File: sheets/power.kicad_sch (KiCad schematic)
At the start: 59 parts, among them J101 USB_C_Receptacle_USB2.0_16P, U102 TPS562201DDCT, U103 TPS562201DDCT, U104 TPS562201DDCT, U201 SAM9X60-V/DWB

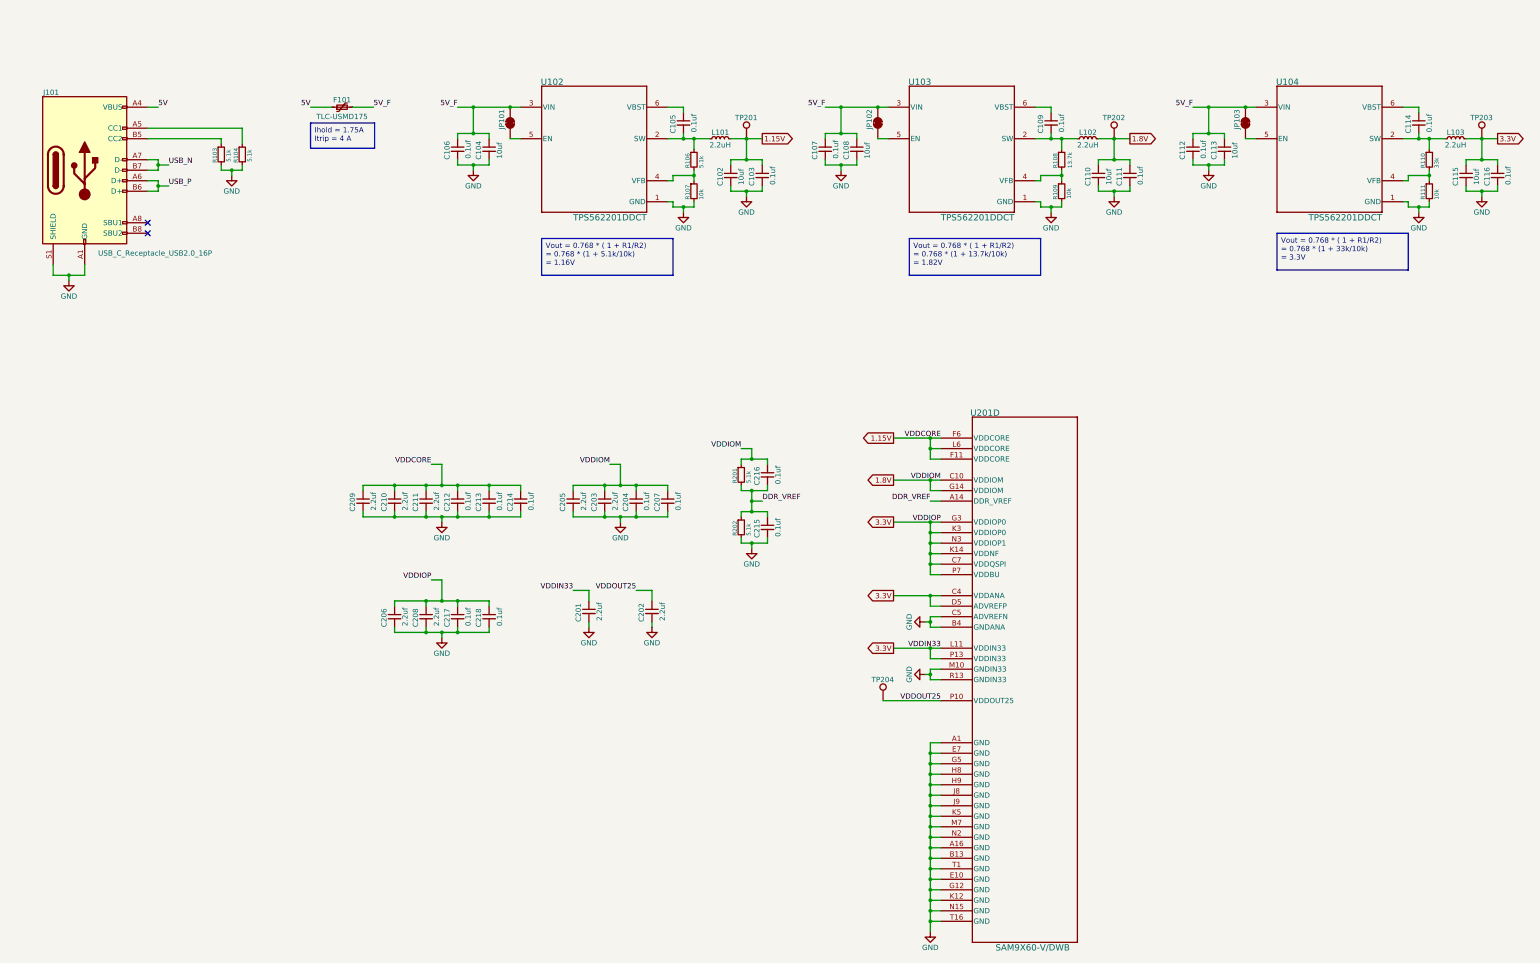
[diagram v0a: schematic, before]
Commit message: Update power schematic
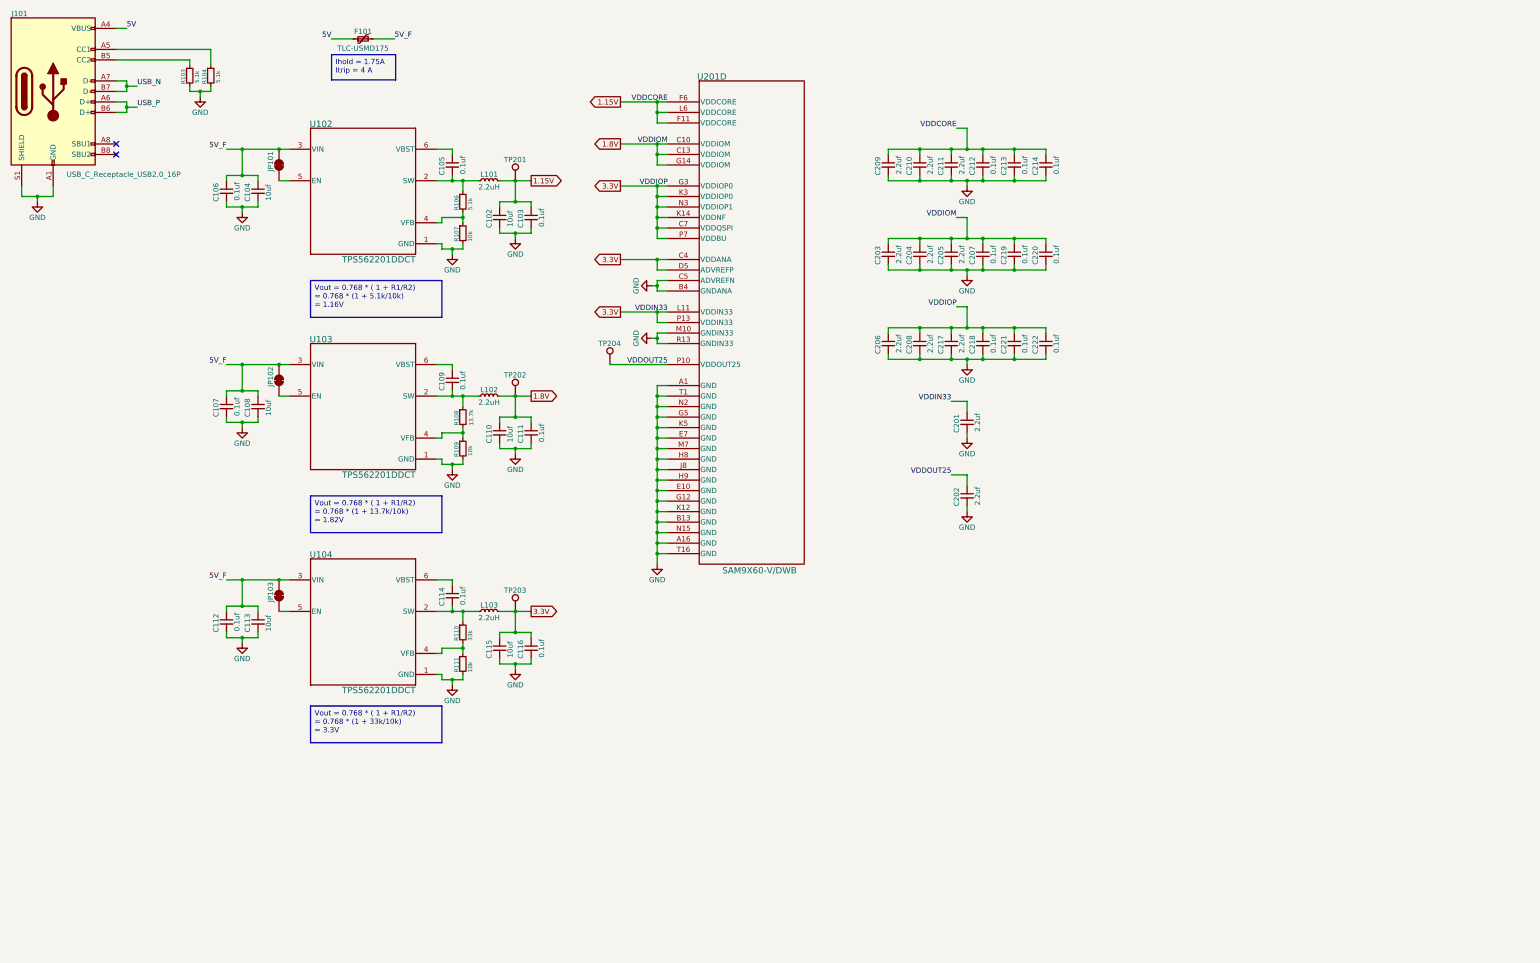
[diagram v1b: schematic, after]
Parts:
- removed C215, C216: 0.1uf, Capacitor_SMD:C_0603_1608Metric_Pad1.08x0.95mm_HandSolder, symbol Device:C_Small
- removed R201, R202: 5.1k, Resistor_SMD:R_0603_1608Metric_Pad0.98x0.95mm_HandSolder, symbol Device:R_Small
- added C219, C220, C221, C222: 0.1uf, Capacitor_SMD:C_0603_1608Metric_Pad1.08x0.95mm_HandSolder, symbol Device:C_Small
- C204, C217: value 0.1uf -> 2.2uf
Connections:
- net 1.8V: now also U201.C13 (VDDIOM), C219.1, C220.1
- net 3.3V: now also C221.1, C222.1
- net GND: now also C219.2, C220.2, C221.2, C222.2; no longer U201.J9 (GND)
- removed net DDR_VREF: U201.A14 (DDR_VREF)
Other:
- moved on the sheet: C102, C103, C104, C105, C106, C107, C108, C109, C110, C111, C112, C113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

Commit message: Finish DRAM schematic
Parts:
- added C223, C224: 2.2uf, Capacitor_SMD:C_0603_1608Metric_Pad1.08x0.95mm_HandSolder, symbol Device:C_Small
- added R203: 10k, Resistor_SMD:R_0603_1608Metric_Pad0.98x0.95mm_HandSolder, symbol Device:R_Small
- C203, C204, C205, C206, C208: value 2.2uf -> 0.1uf
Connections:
- net 1.15V: now also C217.1; no longer C209.1, C210.1
- net 1.8V: now also C210.1, C223.1; no longer C203.1, C204.1, C205.1
- net 3.3V: now also C203.1, C204.1, C205.1, C209.1, C224.1, R203.2; no longer C217.1, U201.D5 (ADVREFP)
- net GND: now also C223.2, C224.2
- new net: R203.1, U201.D5 (ADVREFP)
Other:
- moved on the sheet: C201, C202, C207, C212, C213, C214, C219, C220

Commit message: Update schematic
- Update VDDCORE to 1.13V
- Fix DDR_CAL circuit
- Update external load capacitor to 22pf
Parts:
- R106: value 5.1k -> 4.7k
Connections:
- net 1.15V renamed 1.1V
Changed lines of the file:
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@@
 		(date "2025-07-06")
 	)
+	(text_box "VDDCORE: 1.1V\nVDDIOM: 1.8V\nVDDNF, VDDQSPI, VDDANA, VDDIN33, VDDIOP0, VDDIOP1, VDDBU: 3.3V"
+		(exclude_from_sim no)
+		(at 22.86 93.98 0)
+		(size 40.64 13.97)
+		(margins 0.9525 0.9525 0.9525 0.9525)
+		(stroke
+			(width 0)
+			(type solid)
+		)
+		(fill
+			(type none)
+		)
+		(effects
+			(font
+				(size 1.27 1.27)
+			)
+			(justify left top)
+		)
+	)
 	(text_box "Vout = 0.768 * ( 1 + R1/R2)\n= 0.768 * (1 + 13.7k/10k) \n= 1.82V"
 		(exclude_from_sim no)
@@
 		)
 	)
-	(text_box "Vout = 0.768 * ( 1 + R1/R2)\n= 0.768 * (1 + 5.1k/10k) \n= 1.16V"
+	(text_box "Vout = 0.768 * ( 1 + R1/R2)\n= 0.768 * (1 + 4.7k/10k) \n= 1.13V"
 		(exclude_from_sim no)
 		(at 91.44 81.28 0)
@@
 		)
 	)
-	(global_label "1.15V"
+	(global_label "1.1V"
 		(shape output)
 		(at 166.37 38.1 180)
@@
 		)
 		(property "Intersheetrefs" "${INTERSHEET_REFS}"
-			(at 158.0629 38.1 0)
+			(at 159.2724 38.1 0)
 			(effects
 				(font
@@
 		)
 	)
-	(global_label "1.15V"
+	(global_label "1.1V"
 		(shape output)
 		(at 144.78 57.15 0)
@@
 		)
 		(property "Intersheetrefs" "${INTERSHEET_REFS}"
-			(at 153.0871 57.15 0)
+			(at 151.8776 57.15 0)
 			(effects
 				(font
@@
 			)
 		)
-		(property "Value" "5.1k"
+		(property "Value" "4.7k"
 			(at 130.048 64.262 90)
 			(effects
